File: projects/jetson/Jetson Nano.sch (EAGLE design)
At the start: 19 parts, among them X1 MKDSN1,5/4-5,08, X2 MKDSN1,5/4-5,08

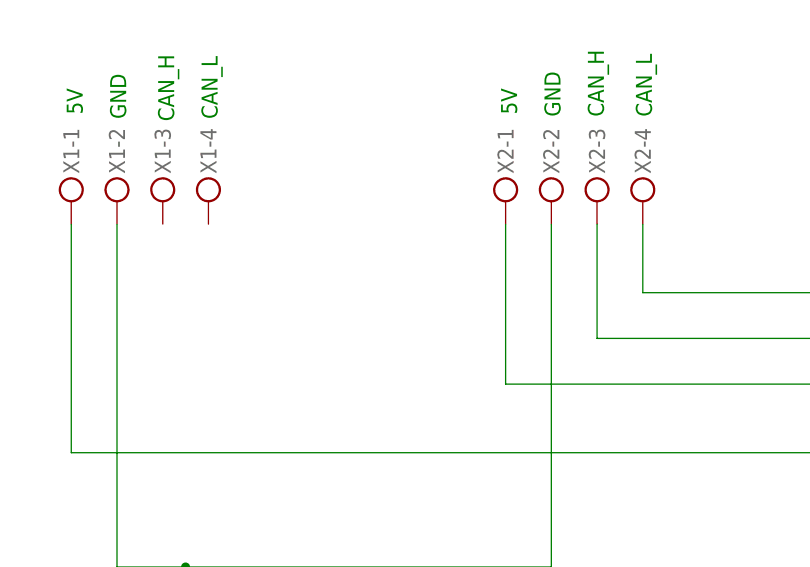
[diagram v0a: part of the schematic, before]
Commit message: create jetson without CAN
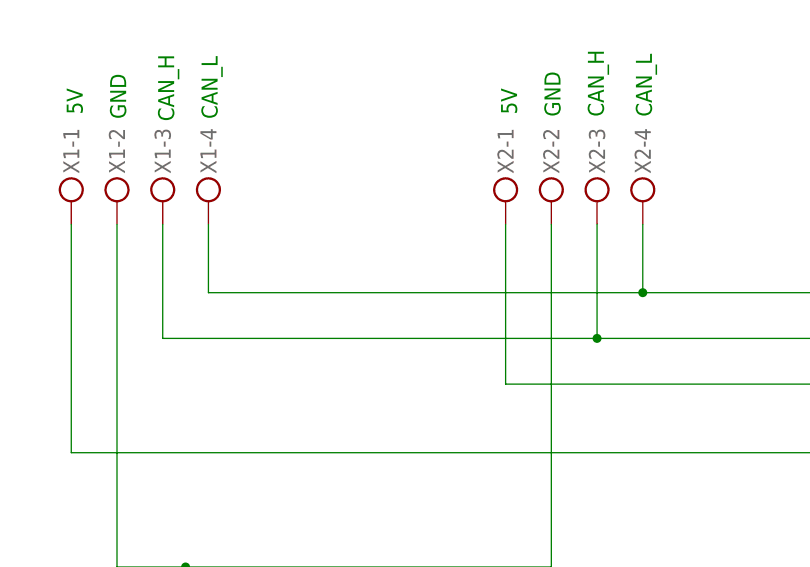
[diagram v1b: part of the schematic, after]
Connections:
- net N$15 renamed CAN_H2
- net N$17 renamed CAN_H3
- net N$18 renamed 3.3V
- removed net N$1: R4.2, X2-4.KL
- removed net N$6: R3.2, X2-3.KL
- new net CAN_H: R3.2, X1-3.KL, X2-3.KL
- new net CAN_L: R4.2, X1-4.KL, X2-4.KL
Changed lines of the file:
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@@
 <clearance class="1" value="0.6604"/>
+</class>
+<class number="2" name="CAN" width="2.032" drill="0">
+<clearance class="2" value="0.6604"/>
 </class>
 </classes>
@@
 </segment>
 </net>
-<net name="N$15" class="0">
+<net name="CAN_H2" class="2">
 <segment>
 <pinref part="U$4" gate="G$1" pin="CANH"/>
@@
 </segment>
 </net>
-<net name="N$17" class="0">
+<net name="CAN_H3" class="2">
 <segment>
 <pinref part="R4" gate="G$1" pin="1"/>
@@
 </segment>
 </net>
-<net name="CAN_INT" class="0">
+<net name="CAN_INT" class="2">
 <segment>
 <pinref part="MCP1" gate="G$1" pin="INT"/>
@@
 </segment>
 </net>
-<net name="N$6" class="0">
+<net name="CAN_H" class="2">
 <segment>
 <pinref part="X2" gate="-3" pin="KL"/>
@@
 <pinref part="R3" gate="G$1" pin="2"/>
 <wire x1="175.26" y1="259.08" x2="144.78" y2="259.08" width="0.1524" layer="91"/>
-</segment>
-</net>
-<net name="N$18" class="0">
+<pinref part="X1" gate="-3" pin="KL"/>
+<wire x1="-71.12" y1="203.2" x2="-71.12" y2="190.5" width="0.1524" layer="91"/>
+<wire x1="-71.12" y1="190.5" x2="-22.86" y2="190.5" width="0.1524" layer="91"/>
+<junction x="-22.86" y="190.5"/>
+</segment>
+</net>
+<net name="3.3V" class="0">
 <segment>
 <pinref part="MCP1" gate="G$1" pin="VDD"/>
@@
 </segment>
 </net>
-<net name="N$1" class="0">
+<net name="CAN_L" class="2">
 <segment>
 <pinref part="X2" gate="-4" pin="KL"/>
@@
 <pinref part="R4" gate="G$1" pin="2"/>
 <wire x1="170.18" y1="256.54" x2="144.78" y2="256.54" width="0.1524" layer="91"/>
-</segment>
-</net>
+<pinref part="X1" gate="-4" pin="KL"/>
+<wire x1="-66.04" y1="203.2" x2="-66.04" y2="195.58" width="0.1524" layer="91"/>
+<wire x1="-66.04" y1="195.58" x2="-17.78" y2="195.58" width="0.1524" layer="91"/>
+<junction x="-17.78" y="195.58"/>
+</segment>
+</net>

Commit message: change all
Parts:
- removed C4: (no value), rcl:C-EU025-024X044
- removed R4: (no value), rcl:R-EU_0207/10
- removed S1, S2: (no value), switch-dil:DS01E
- removed X1, X2: MKDSN1,5/4-5,08, con-phoenix-508:MKDSN1,5/4-5,08
- added 5VIN1, 5VIN2, CAN1, CAN2: (no value), TB113-2B-x-x-0-x-x:2PIN
- added R5, R6: (no value), rcl:R-EU_0207/10
- added SW: SRIDE_SWITCH, Sride Switch:SRIDE_SWITCH
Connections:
- removed net 3.3V: C3.1, JN1.3V3-1, MCP1.VDD, R1.2, U$1.VCC, U$2.1, U$3.3.3V, U$4.VDD
- removed net 5V_1: JN1.5V-1, U$3.5V, X1-1.KL
- removed net CAN_H: R3.2, X1-3.KL, X2-3.KL
- removed net CAN_H3: C4.1, R2.2, R3.1, R4.1, S1.2, S2.2
- removed net CAN_L: R4.2, X1-4.KL, X2-4.KL
- new net +3V3: JN1.3V3-1, MCP1.VDD, R1.2, R5.2, R6.2, U$1.VCC, U$2.1, U$3.3.3V
- new net +5V: 5VIN1.P$1, C3.1, JN1.5V-1, U$3.5V, U$4.VDD
- new net N$1: R2.2
- new net N$15: R3.2, SW.R
- net 5V_2: now also 5VIN2.P$1; no longer X2-1.KL
- net CAN_H2: now also CAN1.P$1, CAN2.P$1, SW.LR; no longer S1.1
- net CAN_INT: now also R5.1
- net N$16: now also CAN1.P$2, CAN2.P$2, R3.1; no longer S2.1
- net N$2: now also 5VIN1.P$2, 5VIN2.P$2; no longer U$3.GND, X1-2.KL, X2-2.KL
- net SS: now also R6.1
- net V-: no longer C4.2
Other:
- moved on the sheet: C1, C2, C3, R1, R2, R3

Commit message: Autoroute Jetson Board
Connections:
- net +5V renamed +5V_1
- net N$2 renamed GND_1
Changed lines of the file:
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@@
 <class number="0" name="default" width="0.6096" drill="0">
 </class>
-<class number="1" name="PW" width="2.032" drill="0">
-<clearance class="1" value="0.6604"/>
+<class number="1" name="PW" width="2.286" drill="0">
+<clearance class="1" value="0.508"/>
 </class>
-<class number="2" name="CAN" width="2.032" drill="0">
-<clearance class="2" value="0.6604"/>
+<class number="2" name="CAN" width="0.6096" drill="0">
+<clearance class="2" value="0.127"/>
 </class>
 </classes>
@@
 </busses>
 <nets>
-<net name="N$2" class="0">
+<net name="GND_1" class="1">
 <segment>
 <pinref part="U$1" gate="G$1" pin="GND"/>
@@
 </segment>
 </net>
-<net name="+5V" class="0">
+<net name="+5V_1" class="1">
 <segment>
 <pinref part="U$3" gate="G$1" pin="5V"/>

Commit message: wakuwaku
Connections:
- removed net GND_1: 5VIN1.P$2, 5VIN2.P$2, JN1.GND-2, U$1.GND, U$1.SDO, U$2.2
- removed net V-: C1.2, C2.1, C3.2, MCP1.VSS, U$4.VSS
- new net GND: 5VIN1.P$2, 5VIN2.P$2, C1.2, C2.1, C3.2, JN1.GND-2, MCP1.VSS, U$1.GND, U$1.SDO, U$2.2, U$3.GND, U$4.VSS
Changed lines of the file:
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@@
 <part name="C1" library="rcl" library_urn="urn:adsk.eagle:library:334" deviceset="C-EU" device="025-024X044" package3d_urn="urn:adsk.eagle:package:23630/1"/>
 <part name="C2" library="rcl" library_urn="urn:adsk.eagle:library:334" deviceset="C-EU" device="025-024X044" package3d_urn="urn:adsk.eagle:package:23630/1"/>
-<part name="P-1" library="supply1" library_urn="urn:adsk.eagle:library:371" deviceset="GND" device=""/>
-<part name="P-2" library="supply1" library_urn="urn:adsk.eagle:library:371" deviceset="GND" device=""/>
-<part name="P-3" library="supply1" library_urn="urn:adsk.eagle:library:371" deviceset="GND" device="">
-<attribute name="GND" value=""/>
-</part>
-<part name="P-4" library="supply1" library_urn="urn:adsk.eagle:library:371" deviceset="GND" device=""/>
 <part name="C3" library="rcl" library_urn="urn:adsk.eagle:library:334" deviceset="C-EU" device="025-024X044" package3d_urn="urn:adsk.eagle:package:23630/1"/>
 <part name="R1" library="rcl" library_urn="urn:adsk.eagle:library:334" deviceset="R-EU_" device="0207/10" package3d_urn="urn:adsk.eagle:package:23491/2"/>
@@
 <part name="5VIN2" library="TB113-2B-x-x-0-x-x" library_urn="urn:adsk.eagle:library:38507486" deviceset="2PIN" device="" package3d_urn="urn:adsk.eagle:package:38507490/6" override_package3d_urn="urn:adsk.eagle:package:38731294/2" override_package_urn="urn:adsk.eagle:footprint:38731295/1"/>
 <part name="CAN2" library="TB113-2B-x-x-0-x-x" library_urn="urn:adsk.eagle:library:38507486" deviceset="2PIN" device="" package3d_urn="urn:adsk.eagle:package:38507490/6" override_package3d_urn="urn:adsk.eagle:package:38731294/2" override_package_urn="urn:adsk.eagle:footprint:38731295/1"/>
+<part name="GND1" library="supply1" library_urn="urn:adsk.eagle:library:371" deviceset="GND" device=""/>
+<part name="GND2" library="supply1" library_urn="urn:adsk.eagle:library:371" deviceset="GND" device=""/>
+<part name="GND3" library="supply1" library_urn="urn:adsk.eagle:library:371" deviceset="GND" device=""/>
+<part name="GND4" library="supply1" library_urn="urn:adsk.eagle:library:371" deviceset="GND" device=""/>
+<part name="GND5" library="supply1" library_urn="urn:adsk.eagle:library:371" deviceset="GND" device=""/>
+<part name="GND6" library="supply1" library_urn="urn:adsk.eagle:library:371" deviceset="GND" device=""/>
+<part name="GND7" library="supply1" library_urn="urn:adsk.eagle:library:371" deviceset="GND" device=""/>
 </parts>
 <sheets>
@@
 <attribute name="VALUE" x="52.324" y="213.741" size="1.778" layer="96"/>
 </instance>
-<instance part="P-1" gate="1" x="43.18" y="215.9" smashed="yes">
-<attribute name="VALUE" x="38.1" y="218.44" size="1.778" layer="96" rot="R270"/>
-</instance>
-<instance part="P-2" gate="1" x="81.28" y="220.98" smashed="yes">
-<attribute name="VALUE" x="76.2" y="223.52" size="1.778" layer="96" rot="R270"/>
-</instance>
-<instance part="P-3" gate="1" x="73.66" y="200.66" smashed="yes">
-<attribute name="VALUE" x="68.58" y="203.2" size="1.778" layer="96" rot="R270"/>
-<attribute name="GND" x="73.66" y="200.66" size="1.778" layer="96" display="off"/>
-</instance>
-<instance part="P-4" gate="1" x="81.28" y="200.66" smashed="yes">
-<attribute name="VALUE" x="71.12" y="203.2" size="1.778" layer="96" rot="R270"/>
-</instance>
 <instance part="C3" gate="G$1" x="73.66" y="205.74" smashed="yes">
 <attribute name="NAME" x="75.184" y="206.121" size="1.778" layer="95"/>
@@
 <instance part="CAN2" gate="G$1" x="-20.32" y="231.14" smashed="yes">
 <attribute name="NAME" x="-22.86" y="236.22" size="1.27" layer="95"/>
+</instance>
+<instance part="GND1" gate="1" x="-60.96" y="99.06" smashed="yes">
+<attribute name="VALUE" x="-63.5" y="96.52" size="1.778" layer="96"/>
+</instance>
+<instance part="GND2" gate="1" x="109.22" y="96.52" smashed="yes">
+<attribute name="VALUE" x="106.68" y="93.98" size="1.778" layer="96"/>
+</instance>
+<instance part="GND3" gate="1" x="81.28" y="200.66" smashed="yes">
+<attribute name="VALUE" x="78.74" y="198.12" size="1.778" layer="96"/>
+</instance>
+<instance part="GND4" gate="1" x="81.28" y="223.52" smashed="yes">
+<attribute name="VALUE" x="78.74" y="220.98" size="1.778" layer="96"/>
+</instance>
+<instance part="GND5" gate="1" x="43.18" y="215.9" smashed="yes">
+<attribute name="VALUE" x="40.64" y="213.36" size="1.778" layer="96"/>
+</instance>
+<instance part="GND6" gate="1" x="73.66" y="198.12" smashed="yes">
+<attribute name="VALUE" x="71.12" y="195.58" size="1.778" layer="96"/>
+</instance>
+<instance part="GND7" gate="1" x="-86.36" y="162.56" smashed="yes">
+<attribute name="VALUE" x="-88.9" y="160.02" size="1.778" layer="96"/>
 </instance>
 </instances>
@@
 </busses>
 <nets>
-<net name="GND_1" class="1">
+<net name="GND" class="1">
 <segment>
 <pinref part="U$1" gate="G$1" pin="GND"/>
@@
 <pinref part="JN1" gate="G$1" pin="GND-2"/>
 <wire x1="-68.58" y1="109.22" x2="-68.58" y2="101.6" width="0.1524" layer="91"/>
-<wire x1="-68.58" y1="101.6" x2="-15.24" y2="101.6" width="0.1524" layer="91"/>
+<wire x1="-68.58" y1="101.6" x2="-60.96" y2="101.6" width="0.1524" layer="91"/>
 <pinref part="U$1" gate="G$1" pin="SDO"/>
+<wire x1="-60.96" y1="101.6" x2="-15.24" y2="101.6" width="0.1524" layer="91"/>
 <wire x1="-101.6" y1="124.46" x2="-68.58" y2="124.46" width="0.1524" layer="91"/>
 <wire x1="-68.58" y1="124.46" x2="-68.58" y2="109.22" width="0.1524" layer="91"/>
@@
 <pinref part="5VIN1" gate="G$1" pin="P$2"/>
 <pinref part="5VIN2" gate="G$1" pin="P$2"/>
+<pinref part="GND1" gate="1" pin="GND"/>
+<junction x="-60.96" y="101.6"/>
+<pinref part="GND7" gate="1" pin="GND"/>
+<junction x="-86.36" y="165.1"/>
+</segment>
+<segment>
+<pinref part="GND2" gate="1" pin="GND"/>
+<wire x1="109.22" y1="99.06" x2="109.22" y2="114.3" width="0.1524" layer="91"/>
+<pinref part="U$3" gate="G$1" pin="GND"/>
+<wire x1="109.22" y1="114.3" x2="116.84" y2="114.3" width="0.1524" layer="91"/>
+</segment>
+<segment>
+<pinref part="U$4" gate="G$1" pin="VSS"/>
+<wire x1="83.82" y1="213.36" x2="81.28" y2="213.36" width="0.1524" layer="91"/>
+<wire x1="81.28" y1="213.36" x2="81.28" y2="203.2" width="0.1524" layer="91"/>
+<pinref part="GND3" gate="1" pin="GND"/>
+</segment>
+<segment>
+<pinref part="MCP1" gate="G$1" pin="VSS"/>
+<wire x1="83.82" y1="228.6" x2="81.28" y2="228.6" width="0.1524" layer="91"/>
+<wire x1="81.28" y1="228.6" x2="81.28" y2="226.06" width="0.1524" layer="91"/>
+<pinref part="GND4" gate="1" pin="GND"/>
+</segment>
+<segment>
+<pinref part="C2" gate="G$1" pin="1"/>
+<pinref part="C1" gate="G$1" pin="2"/>
+<wire x1="50.8" y1="220.98" x2="50.8" y2="223.52" width="0.1524" layer="91"/>
+<junction x="50.8" y="220.98"/>
+<wire x1="43.18" y1="218.44" x2="43.18" y2="220.98" width="0.1524" layer="91"/>
+<wire x1="43.18" y1="220.98" x2="50.8" y2="220.98" width="0.1524" layer="91"/>
+<pinref part="GND5" gate="1" pin="GND"/>
+</segment>
+<segment>
+<pinref part="C3" gate="G$1" pin="2"/>
+<wire x1="73.66" y1="200.66" x2="73.66" y2="203.2" width="0.1524" layer="91"/>
+<pinref part="GND6" gate="1" pin="GND"/>
+<junction x="73.66" y="200.66"/>
 </segment>
 </net>
@@
 </segment>
 </net>
-<net name="V-" class="0">
-<segment>
-<pinref part="C2" gate="G$1" pin="1"/>
-<pinref part="C1" gate="G$1" pin="2"/>
-<wire x1="50.8" y1="220.98" x2="50.8" y2="223.52" width="0.1524" layer="91"/>
-<junction x="50.8" y="220.98"/>
-<pinref part="P-1" gate="1" pin="GND"/>
-<wire x1="43.18" y1="218.44" x2="43.18" y2="220.98" width="0.1524" layer="91"/>
-<wire x1="43.18" y1="220.98" x2="50.8" y2="220.98" width="0.1524" layer="91"/>
-</segment>
-<segment>
-<pinref part="MCP1" gate="G$1" pin="VSS"/>
-<pinref part="P-2" gate="1" pin="GND"/>
-<wire x1="83.82" y1="228.6" x2="81.28" y2="228.6" width="0.1524" layer="91"/>
-<wire x1="81.28" y1="228.6" x2="81.28" y2="223.52" width="0.1524" layer="91"/>
-</segment>
-<segment>
-<pinref part="C3" gate="G$1" pin="2"/>
-<pinref part="P-3" gate="1" pin="GND"/>
-<wire x1="73.66" y1="200.66" x2="73.66" y2="203.2" width="0.1524" layer="91"/>
-</segment>
-<segment>
-<pinref part="U$4" gate="G$1" pin="VSS"/>
-<pinref part="P-4" gate="1" pin="GND"/>
-<wire x1="83.82" y1="213.36" x2="81.28" y2="213.36" width="0.1524" layer="91"/>
-<wire x1="81.28" y1="213.36" x2="81.28" y2="203.2" width="0.1524" layer="91"/>
-</segment>
-</net>
